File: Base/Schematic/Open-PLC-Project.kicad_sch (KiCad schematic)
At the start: 0 parts

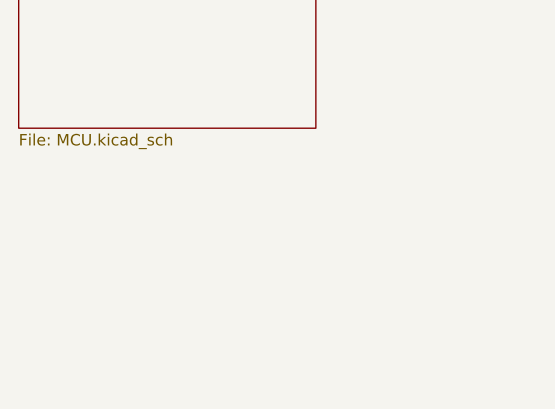
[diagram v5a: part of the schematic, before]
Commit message: [Base PCB 업데이트] - PCB 외곽선과 볼트 위치 설정
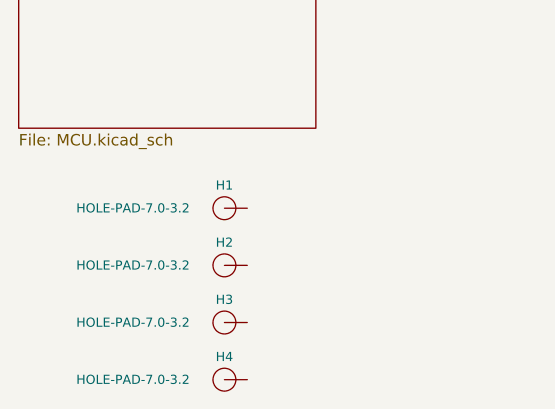
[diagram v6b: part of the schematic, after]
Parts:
- added H1, H2, H3, H4: HOLE-PAD-7.0-3.2, Hole:Hole_7_0_3_2, symbol HOLE:HOLE-PAD-7.0-3.2

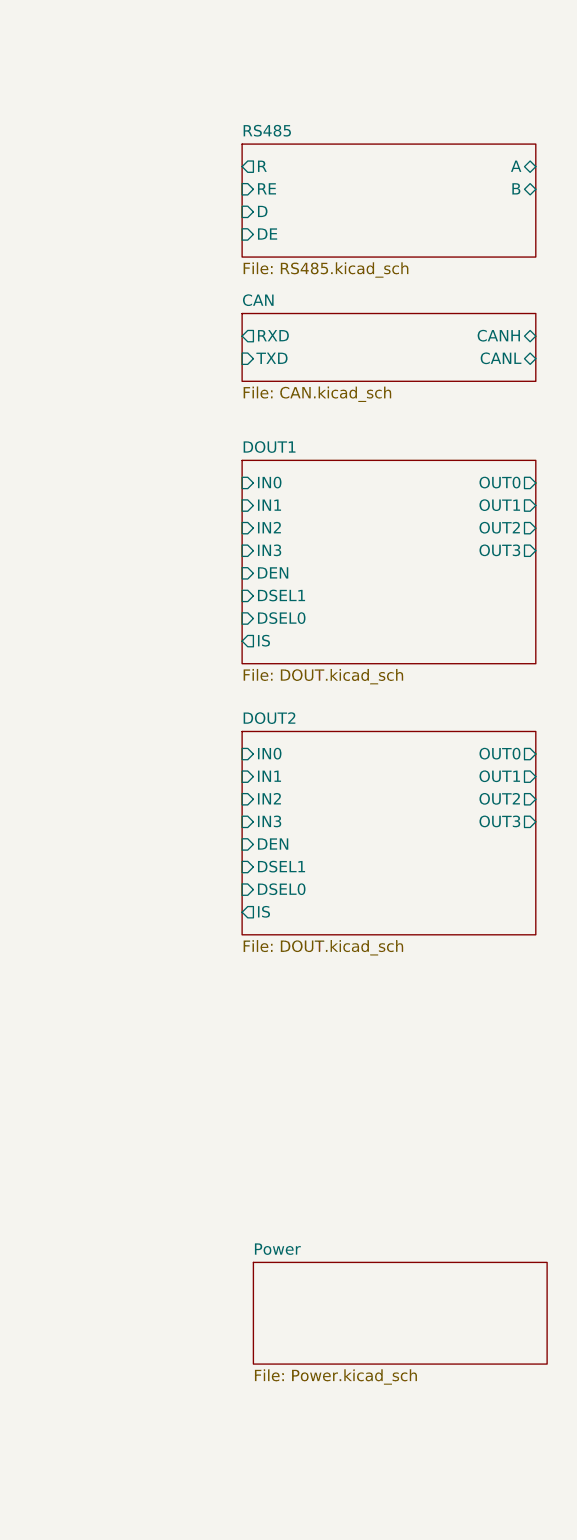
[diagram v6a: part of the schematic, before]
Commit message: [Base 회로도 업데이트] - DIN 입력 8개 추가
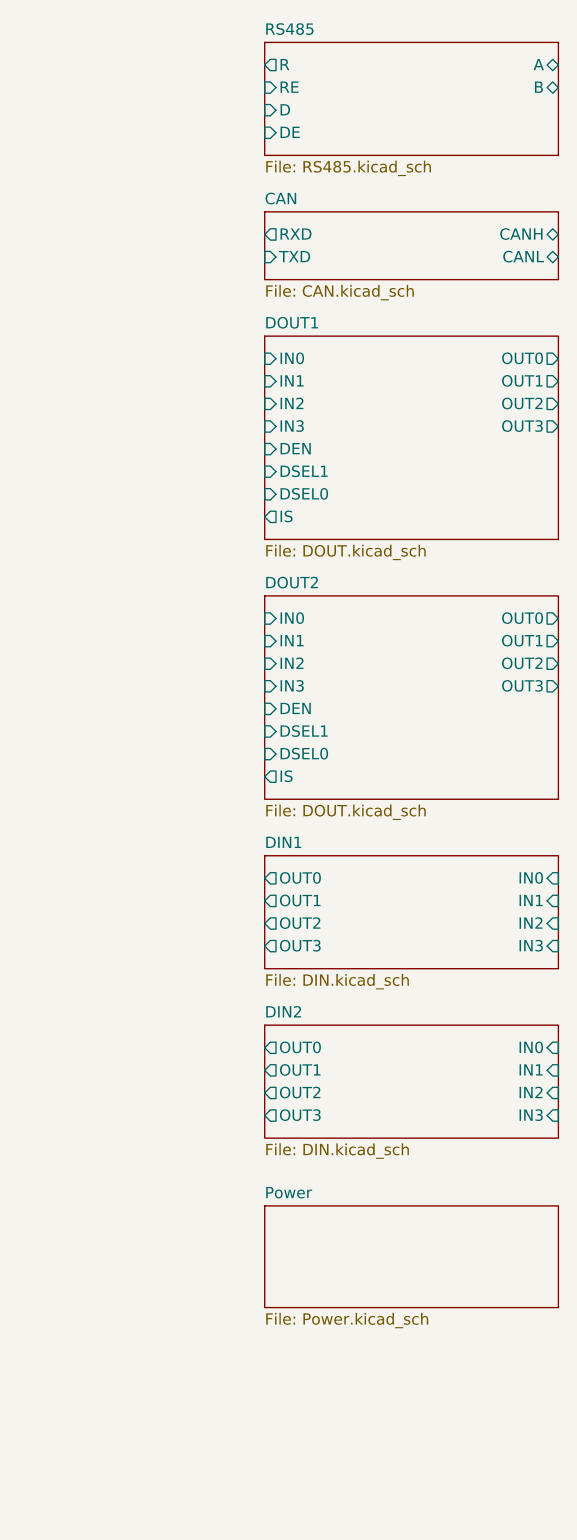
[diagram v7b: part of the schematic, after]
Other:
- added sheet DIN1 (DIN.kicad_sch)
- added sheet DIN2 (DIN.kicad_sch)

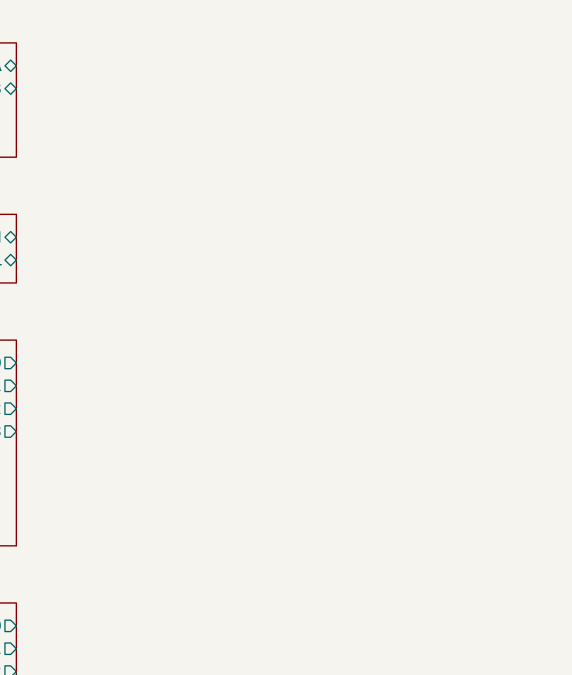
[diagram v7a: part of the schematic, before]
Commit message: [Base 회로도 업데이트] - AIN 입력 4개 추가
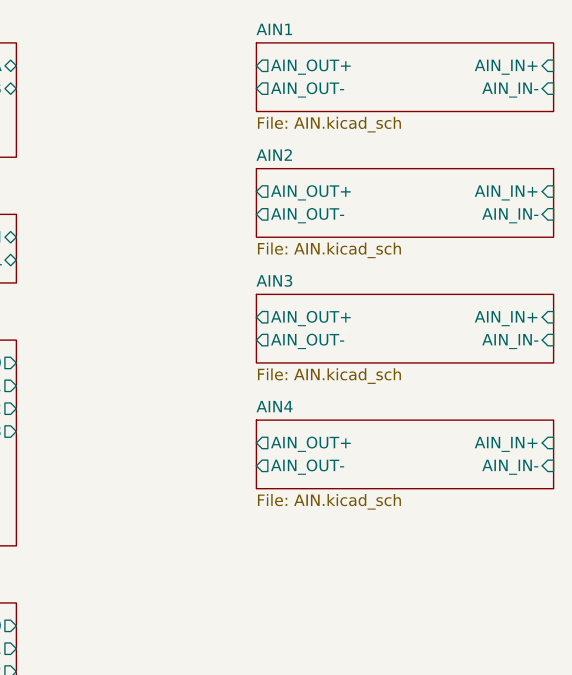
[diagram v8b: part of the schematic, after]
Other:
- added sheet AIN1 (AIN.kicad_sch)
- added sheet AIN2 (AIN.kicad_sch)
- added sheet AIN3 (AIN.kicad_sch)
- added sheet AIN4 (AIN.kicad_sch)
